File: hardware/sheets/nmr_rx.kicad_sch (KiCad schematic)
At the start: 92 parts, among them J3 C2937625_-_Conn_01x03, J9 C2937625_-_Conn_01x03, U701 SI5351A-B-GT, U702 74HC74D,653, U703 OPA1656IDR, U704 DG419DY-T1-E3, U705 OPA1612AIDR, U706 OPA1612AIDR, U901 TS5A23157DGSR, U902 TS5A23157DGSR, Y701 25 MHz

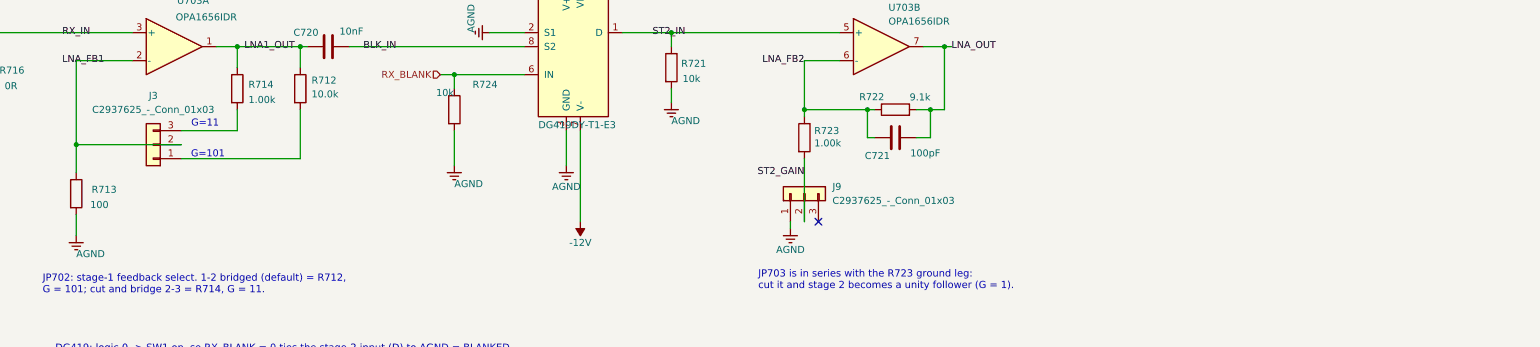
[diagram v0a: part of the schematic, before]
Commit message: Schematic review fixes, part 2 (Konnect): panel RX/AUX labels + SMA labels swapped to match the main board (copper unchanged); TX_VMID -> R820 47k -> TX_IN (C810 couples into TX_IN); Q901 D/S corrected + D932 to +VEXT; R950 10k Q904 gate-source; R712 permanent (J3 pin 1 tied to pin 2); U302/C308 on +5VA; panel 6N137 VCC/VE + C401/C402 on +5V_RAW; R521-R528 DIO pull-downs; front_panel_link sheet removed from the root; change notes on six sheets; panel silk: pairing labels corrected, stale J3 texts deleted, TX/RX/AUX labels fixed, OUT1..7. ERC unchanged (2 cosmetic), panel DRC 0/0; netlist diff = intended changes only
Co-Authored-By: Claude Fable 5.1 <noreply@anthropic.com>
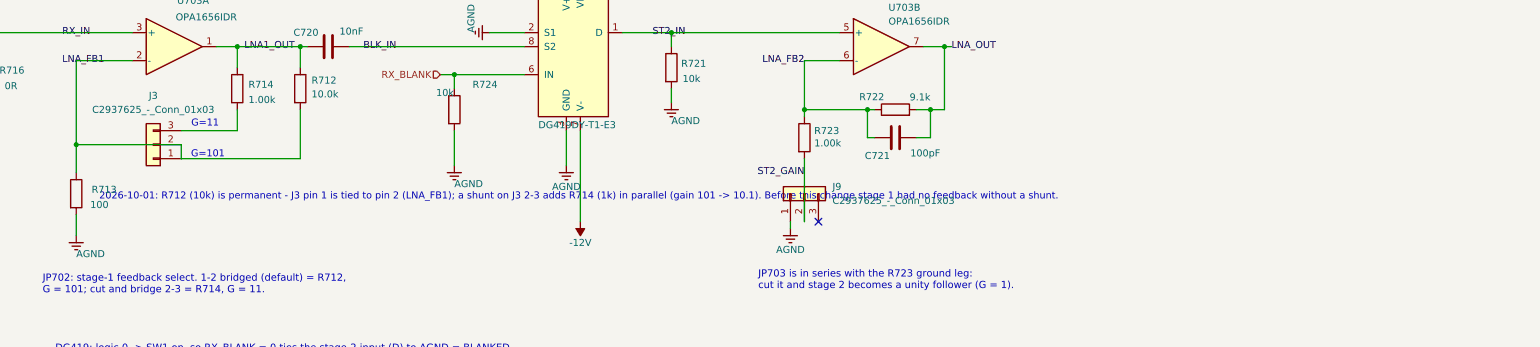
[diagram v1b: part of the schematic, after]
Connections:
- net LNA_FB1: now also J3.1 (Pin_1), R712.2
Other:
- note added: "2026-10-01: R712 (10k) is permanent - J3 pin 1 is tied to pin 2 (LNA_FB1); a shunt on J3 2-3 adds R714 (1k) in parallel (gain 101 -> 10.1). Before this change stage 1 had no feedback without a shunt."

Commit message: hardware: instructor 2026-10-01 saves synced (one GND net on both boards, PCB updated, R951-R958, headers DNP per Decision #73) + nmr_tx R808 -> TX_VMID, C813 removed, R805/R806 10 k (review B2)
Co-Authored-By: Claude Fable 5.1 <noreply@anthropic.com>
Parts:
- J3, J9: now not fitted; now left out of the parts list
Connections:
- net AGND is gone; now on net GND: C706.2, C707.2, C710.1, C711.1, C712.1, C722.2, C723.2, C724.2, C725.2, C726.2, C727.2, C905.2, C906.2, C907.2, C908.2, C916.2, C917.2, C918.2, C919.2, D703.1 (K), D704.2 (A), D905.1 (A1), D906.1 (A1), D907.1 (A1), D908.1 (A1), J9.1 (Pin_1), R711.1, R713.2, R716.1, R721.2, R724.2, R904.2, R917.2, R924.2, U702.7 (GND), U704.2 (S1), U704.3 (GND), U705.3 (+), U901.3 (GND), U902.3 (GND)
- net LNA_FB1: no longer J3.1 (Pin_1), R712.2
- new net: J3.1 (Pin_1), R712.2

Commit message: Instructor 2026-10-01 afternoon saves (after the review: Update PCB for the nmr_tx change and further sheet edits); ignore the board STEP export
Co-Authored-By: Claude Fable 5.1 <noreply@anthropic.com>
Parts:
- J3, J9: now fitted; now in the parts list
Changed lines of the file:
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@@
 		(body_style 1)
 		(exclude_from_sim no)
-		(in_bom no)
+		(in_bom yes)
 		(on_board yes)
 		(in_pos_files yes)
-		(dnp yes)
+		(dnp no)
 		(fields_autoplaced yes)
 		(property "Reference" "J9"
@@
 		(body_style 1)
 		(exclude_from_sim no)
-		(in_bom no)
+		(in_bom yes)
 		(on_board yes)
 		(in_pos_files yes)
-		(dnp yes)
+		(dnp no)
 		(fields_autoplaced yes)
 		(property "Reference" "J3"

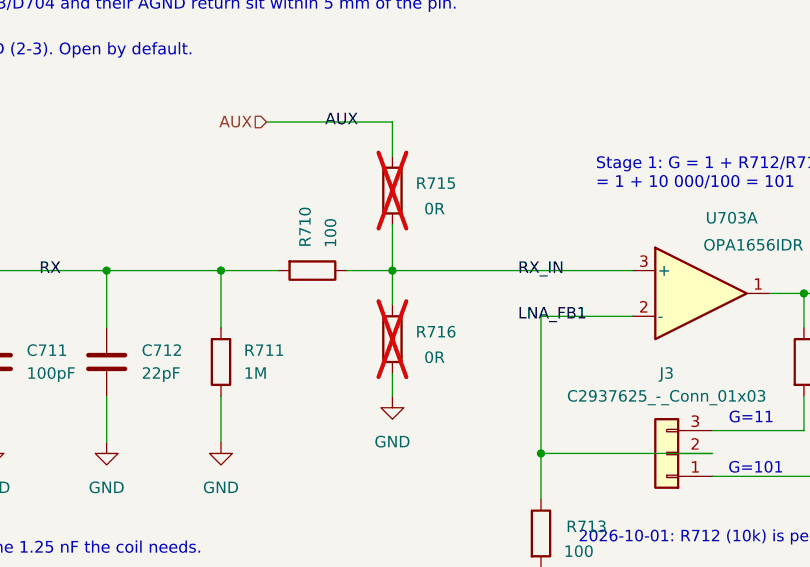
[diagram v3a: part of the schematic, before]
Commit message: Boards as ordered: instructor saves 2026-10-05 04:34 (J1/R1/R2/TP1/FID3 nudged, DNP flags on D934 R715 R716 R811 R812), JLC production files 04:03/04:04
Co-Authored-By: Claude Fable 5.1 <noreply@anthropic.com>
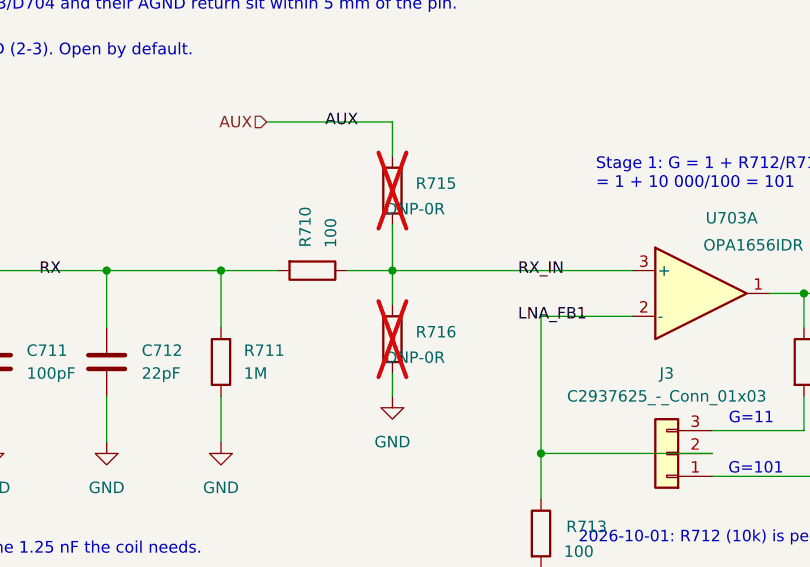
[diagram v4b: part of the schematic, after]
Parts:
- R715, R716: value 0R -> DNP-0R
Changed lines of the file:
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@@
 			)
 		)
-		(property "Value" "0R"
+		(property "Value" "DNP-0R"
 			(at 153.162 199.644 0)
 			(show_name no)
@@
 			)
 		)
-		(property "Value" "0R"
+		(property "Value" "DNP-0R"
 			(at 153.162 216.154 0)
 			(show_name no)
